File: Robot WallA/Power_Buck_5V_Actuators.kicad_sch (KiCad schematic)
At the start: 19 parts, among them Q6 BSS138, U9 PTN78060W_EUW-7

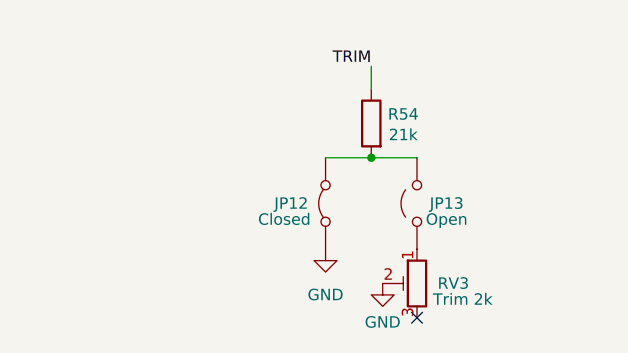
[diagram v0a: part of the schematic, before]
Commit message: Added diode for Type-C connector in case we accidentally power the board with this connector.
Updated fab files
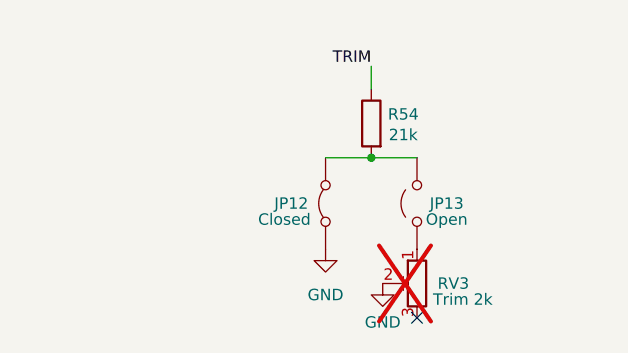
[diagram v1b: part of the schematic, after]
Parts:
- RV3: now not fitted
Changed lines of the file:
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@@
 		(in_bom yes)
 		(on_board yes)
-		(dnp no)
+		(dnp yes)
 		(property "Reference" "RV3"
 			(at 251.206 124.46 0)

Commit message: Modified footprint to simplify BOM. Finalized BOM.
Updated fab files
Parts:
- C119: Manufacturer_Part_Number (none) -> CL21B103KBANNNC
- C121, C122, C123: value 47nF/25V -> 47nF/50V; Manufacturer_Part_Number (none) -> CC0603KPX7R9BB473
- C124, C125: value 4.7uF/25V -> 4.7uF/50V
- C86: Manufacturer_Part_Number (none) -> EEU-FC1V101
- JP12: now left out of the parts list
- R30: Manufacturer_Part_Number (none) -> ERJ-3EKF1601V
- R54: Manufacturer_Part_Number (none) -> RC0603FR-0721KL
- R60: Manufacturer_Part_Number (none) -> 667-ERJ-3GEYJ103V
